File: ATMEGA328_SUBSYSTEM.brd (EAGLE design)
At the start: 30 parts, among them IC1 FT232RL, J5 MINI-USB-UX60A-MB-5ST, U1 ATMEGA328P-AUR, U4 MCP1703CB

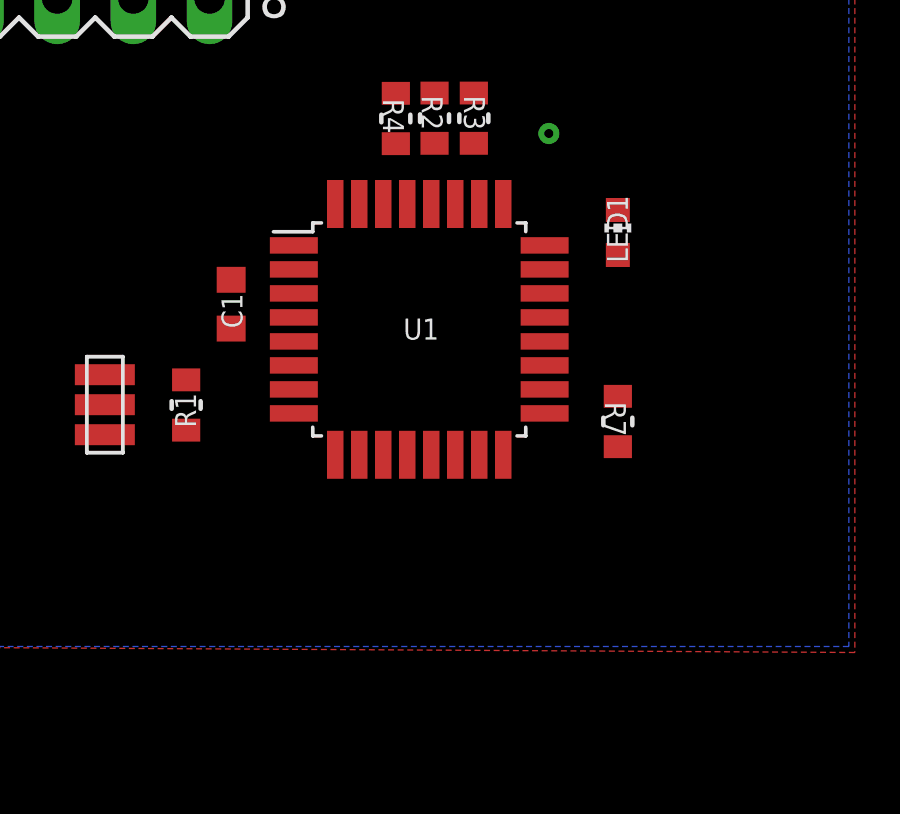
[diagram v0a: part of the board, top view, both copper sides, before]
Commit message: Deleted backup files
Deleted backups of the design, not needed
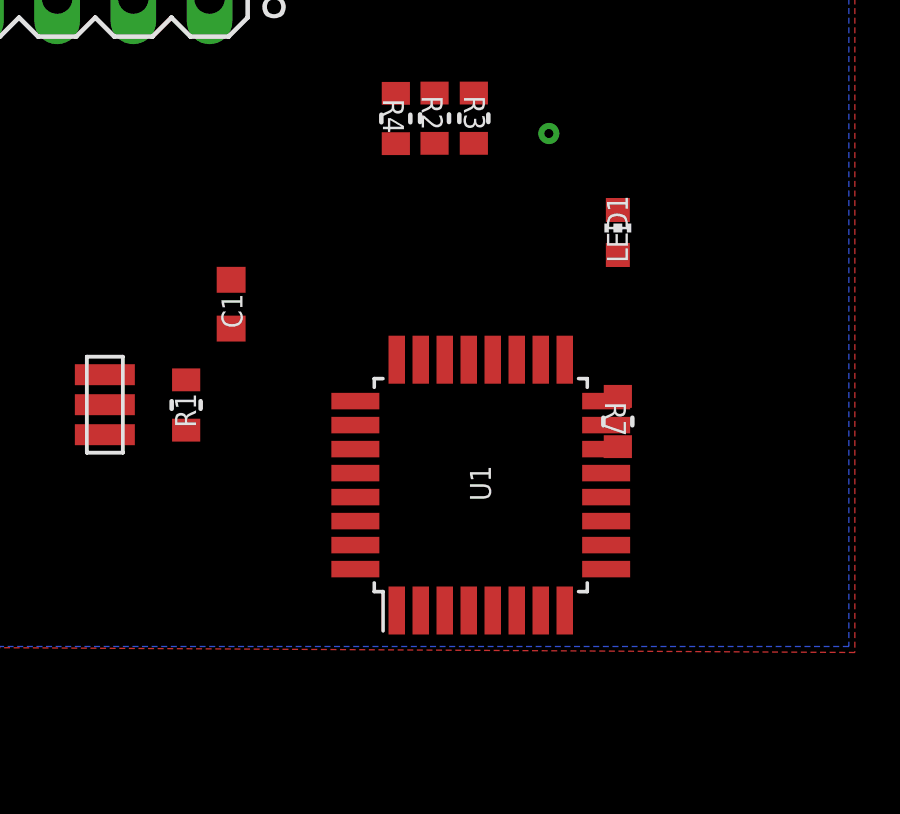
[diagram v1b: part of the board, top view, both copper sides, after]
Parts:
- moved U1 5.58 mm to (41.7, 6.28), turned to 0 degrees
